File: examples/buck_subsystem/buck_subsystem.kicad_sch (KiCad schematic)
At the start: 4 parts, among them U1 TPS562201

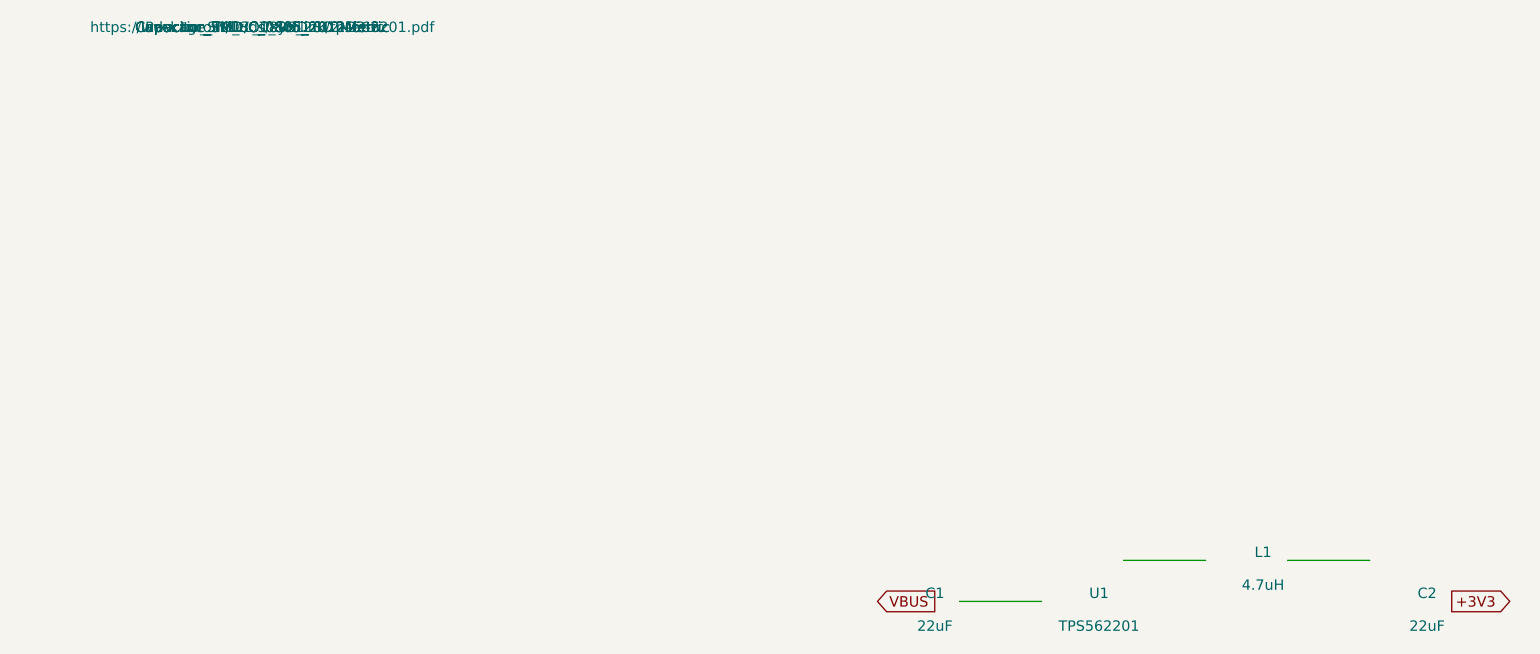
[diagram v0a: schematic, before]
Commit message: feat(libs): pinned bundled KiCad mirror + real-part example fixups (T9)
Lands the bundled symbol/footprint mirror SPEC §9.5/§12/D6/FR-040 require.
libs/ ships a curated, pinned subset of the official KiCad libraries — the
five whole symbol libs the examples reference (Device, power, Connector,
Regulator_Switching, RF_Module) plus the exact footprints they place — all
fetched from KiCad GitLab at tag 9.0.0 and SHA-256-pinned in MANIFEST.toml by
scripts/populate_libs.py (--pin re-fetches+repins; default verifies and
self-heals missing files per D6). sym-lib-table/fp-lib-table register them via
${KICLAUDE_BUNDLED_LIBS}; LICENSE.md carries the CC-BY-SA-4.0 + KiCad Library
Exception attribution.

kiserver GET /project/{id}/library/search now resolves the project's own libs
AND the bundled mirror (bundled_libs_dir() + _merge_hits), so a project with an
empty sym-lib-table still resolves the standard KiCad parts offline. Empirical
gate: Device:R and Connector:USB_C_* resolve through the route (9 tests).

Fixes the examples' fictional/wrong library references to real KiCad 9.0.0
parts (the mirror cannot honestly contain libraries KiCad does not ship):
- blinky: MCU_Espressif: -> RF_Module:ESP32-S3-WROOM-1
- esp32_c6_rf: ESP32-C6-WROOM-1 -> ESP32-C6-MINI-1; fabricated
  Package_BGA:DDR3L_BGA-16_4x4_P0.8mm -> real BGA-16_1.92x1.92mm_Layout4x4_P0.5mm
  (Value MT41K256M16-DDR3L -> BGA-16, that DRAM is FBGA-96); U.FL ->
  Connector_Coaxial:U.FL_Molex_MCRF_73412-0110_Vertical
- buck_subsystem: Regulator_Switching:TPS562201 -> pin-identical real TPS562202
  (+ matching TI datasheet URL)

Golden round-trip (M0-Q-02) + snapshot re-verified byte-identical.

Co-Authored-By: Claude Opus 4.7 (1M context) <noreply@anthropic.com>
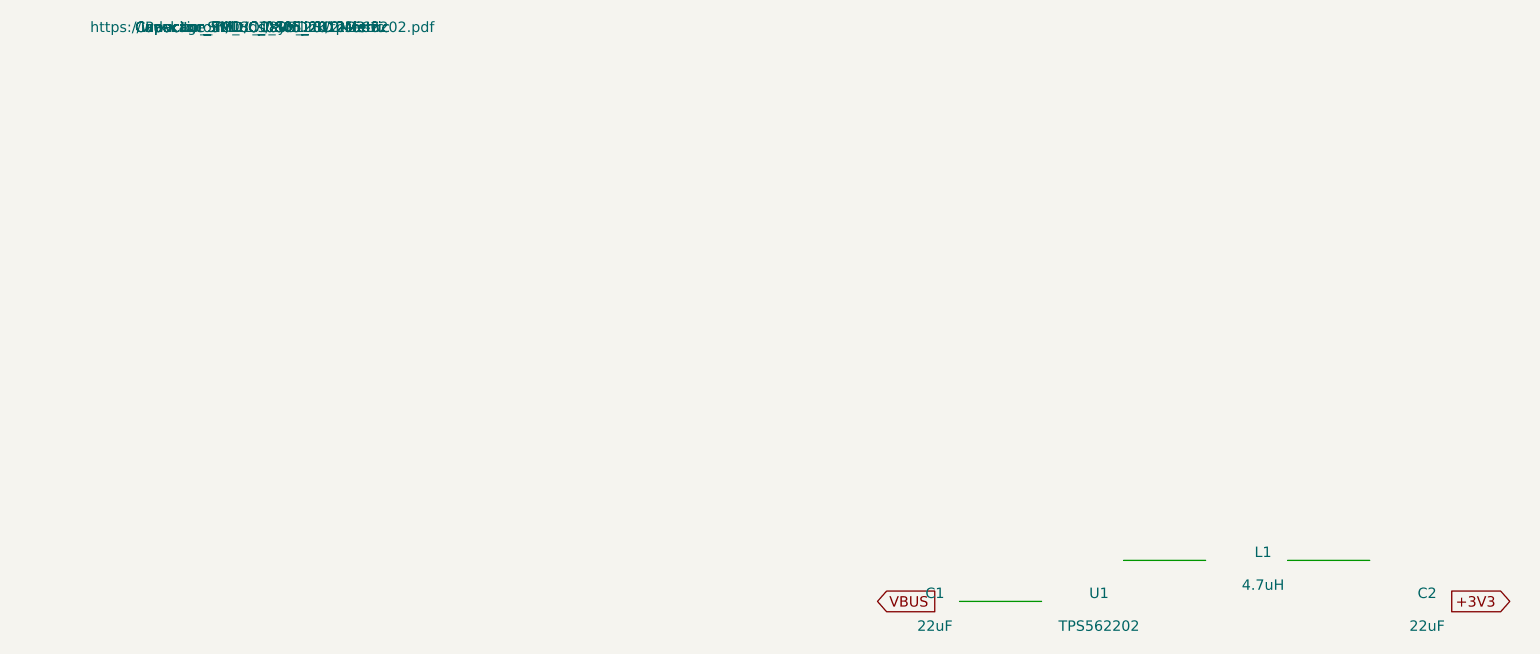
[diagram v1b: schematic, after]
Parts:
- U1: value TPS562201 -> TPS562202; symbol Regulator_Switching:TPS562201 -> Regulator_Switching:TPS562202
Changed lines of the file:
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@@
     (company "")
   )
-  (symbol (lib_id "Regulator_Switching:TPS562201") (at 100.0 70.0 0) (unit 1) (in_bom yes) (on_board yes)
+  (symbol (lib_id "Regulator_Switching:TPS562202") (at 100.0 70.0 0) (unit 1) (in_bom yes) (on_board yes)
     (property "Reference" "U1" (at 102 69 0))
-    (property "Value" "TPS562201" (at 102 73 0))
+    (property "Value" "TPS562202" (at 102 73 0))
     (property "Footprint" "Package_TO_SOT_SMD:SOT-23-6" (at 0 0 0))
-    (property "Datasheet" "https://www.ti.com/lit/ds/symlink/tps562201.pdf" (at 0 0 0))
+    (property "Datasheet" "https://www.ti.com/lit/ds/symlink/tps562202.pdf" (at 0 0 0))
   )
   (symbol (lib_id "Device:C") (at 80.0 70.0 0) (unit 1) (in_bom yes) (on_board yes)
